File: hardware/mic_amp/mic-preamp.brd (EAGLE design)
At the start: 50.5 x 34.3 mm, 16 parts

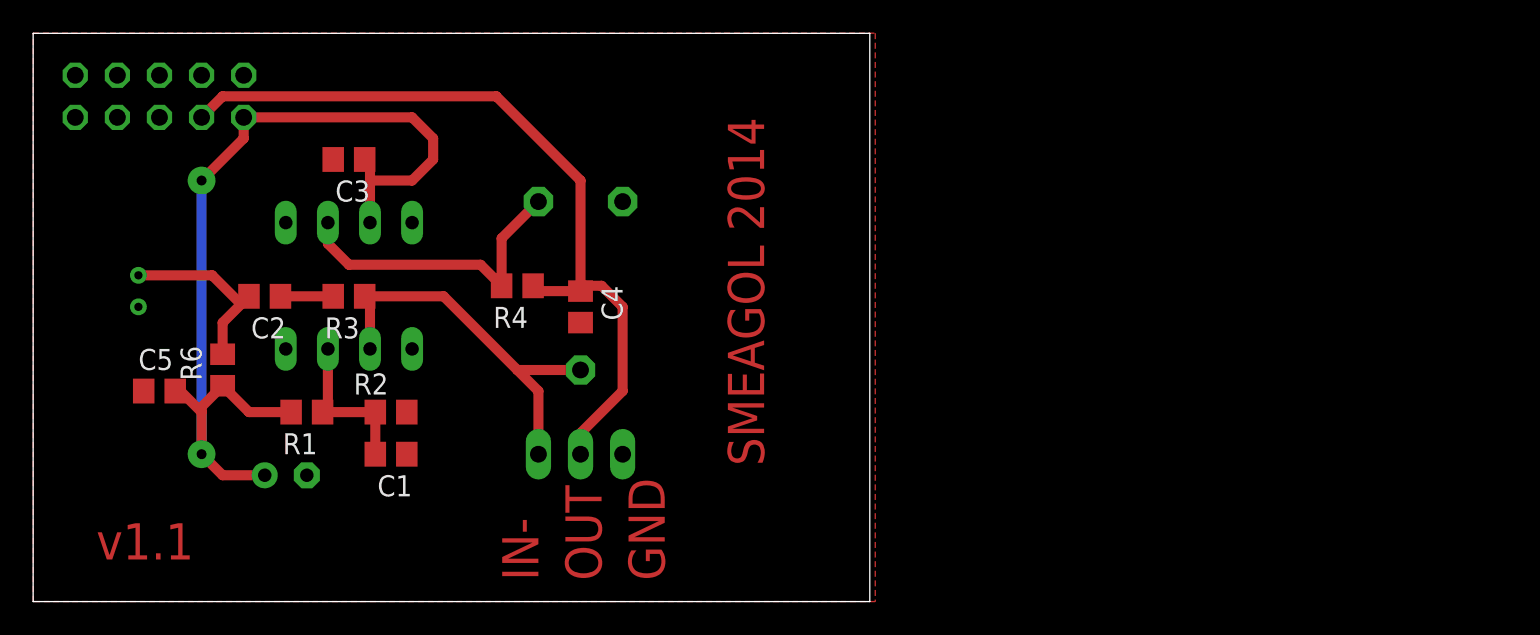
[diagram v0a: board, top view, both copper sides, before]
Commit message: modified mic-amp for better noise immunity
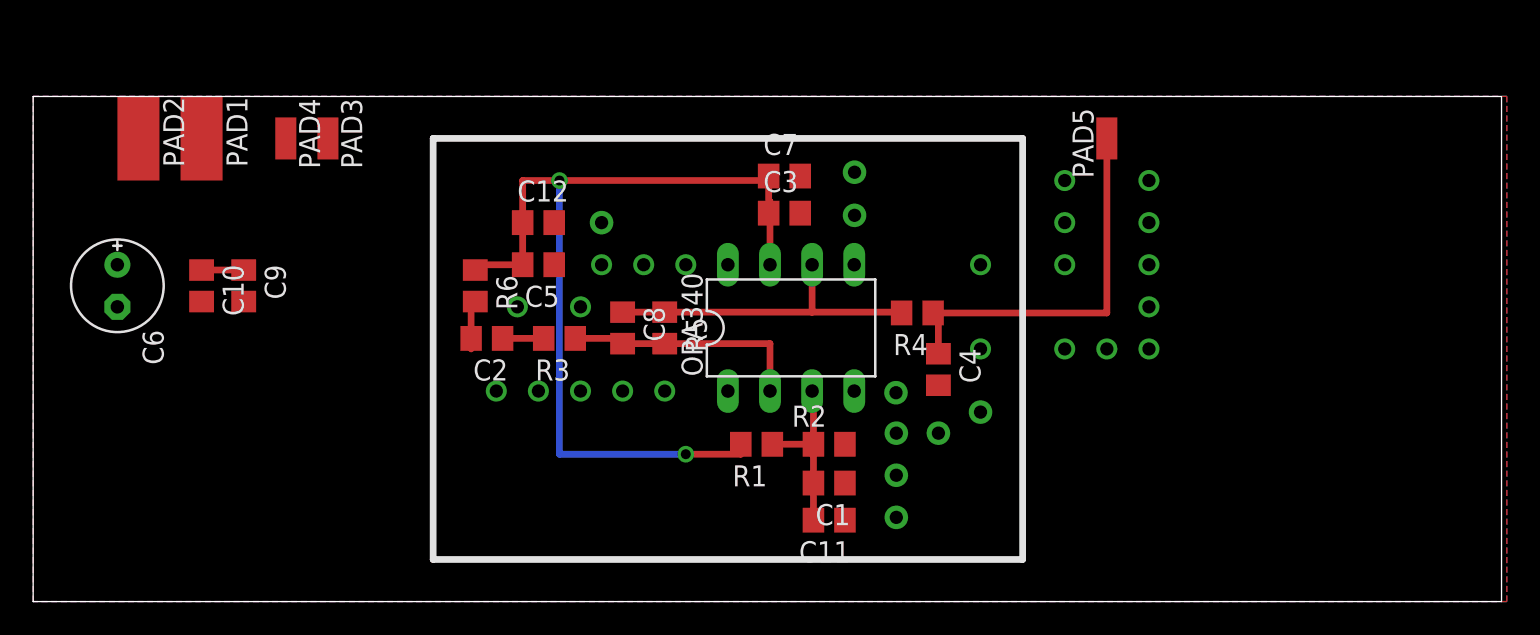
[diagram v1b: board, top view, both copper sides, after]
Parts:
- removed JP1: (no value), pinhead:1X03
- removed JP2: (no value), pinhead:2X05
- removed MIC: MKD-1318, mic:MIC
- removed R_GAIN: 100k, rcl:PT-10
- added C10: 1u, rcl:C0805
- added C11, C12, C7: 100p, rcl:C0805
- added C8: 500p, rcl:C0805
- added C9: 0.1u, rcl:C0805
- added PAD1, PAD2: (no value), wirepad:SMD2,54-5,08
- added PAD3, PAD4, PAD5: WIREPADSMD1,27-254, wirepad:SMD1,27-2,54
- added R5: 50k, rcl:R0805
- C6: value (none) -> 10u
- moved R1 27.2 mm to (43.6, 9.49)
- moved OPA340 26.8 mm to (45.7, 16.5), flipped to the top
- moved R2 26.5 mm to (48.0, 9.49)
- moved C1 26.5 mm to (48.0, 7.15)
- moved C3 26.5 mm to (45.3, 23.4), turned to 0 degrees
- moved R4 24.2 mm to (53.3, 17.4)
- moved C5 24.1 mm to (30.5, 20.3), turned to 180 degrees
- moved C4 21.9 mm to (54.6, 14.0)
- moved R6 16.1 mm to (26.7, 19.1), turned to 270 degrees
- moved C6 15.3 mm to (5.08, 19.1), flipped to the top, turned to 270 degrees
- moved C2 13.6 mm to (27.4, 15.9)
- moved R3 13.0 mm to (31.8, 15.9)
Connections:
- removed net OPAIN: JP1.3, OPA340.2, R3.1, R_GAIN.3
- new net GNDIN: PAD1.1
- new net N$5: C8.2, OPA340.2, R3.1, R5.2
- new net VCCIN: PAD2.1
- net GND: now also C10.2, C11.1, C12.2, C7.2, C9.2, PAD3.1; no longer C6.-, JP1.1, JP2.9, MIC.OUT
- net MIC: now also PAD4.1; no longer MIC.IN
- net N$1: now also C8.1, R5.1; no longer R_GAIN.1
- net N$2: now also C11.2
- net OUT: now also PAD5.1; no longer JP1.2, JP2.3
- net VCC: now also C10.1, C12.1, C7.1, C9.1; no longer C6.+, JP2.1
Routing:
- net OUT: track 48.3 -> 23.5 mm
- net OPAIN: track 24.2 -> 0.00 mm
- net N$5: track 0.00 -> 14.9 mm
- net MIC: track 11.1 -> 3.11 mm
- net VCC: track 58.8 -> 61.3 mm
- net N$2: track 9.66 -> 10.9 mm
- net N$1: track 18.8 -> 19.7 mm
- net N$4: track 3.18 -> 2.48 mm
- added copper zone on layer 16, net GND
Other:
- board size 50.5 x 34.3 mm -> 88.6 x 30.5 mm
- board text removed: "GND"
- board text removed: "IN-"
- board text removed: "OUT"
- board text removed: "SMEAGOL 2014"
- board text removed: "v1.1"
